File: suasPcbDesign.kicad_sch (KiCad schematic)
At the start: 10 parts, among them U1 LMR51625DDC

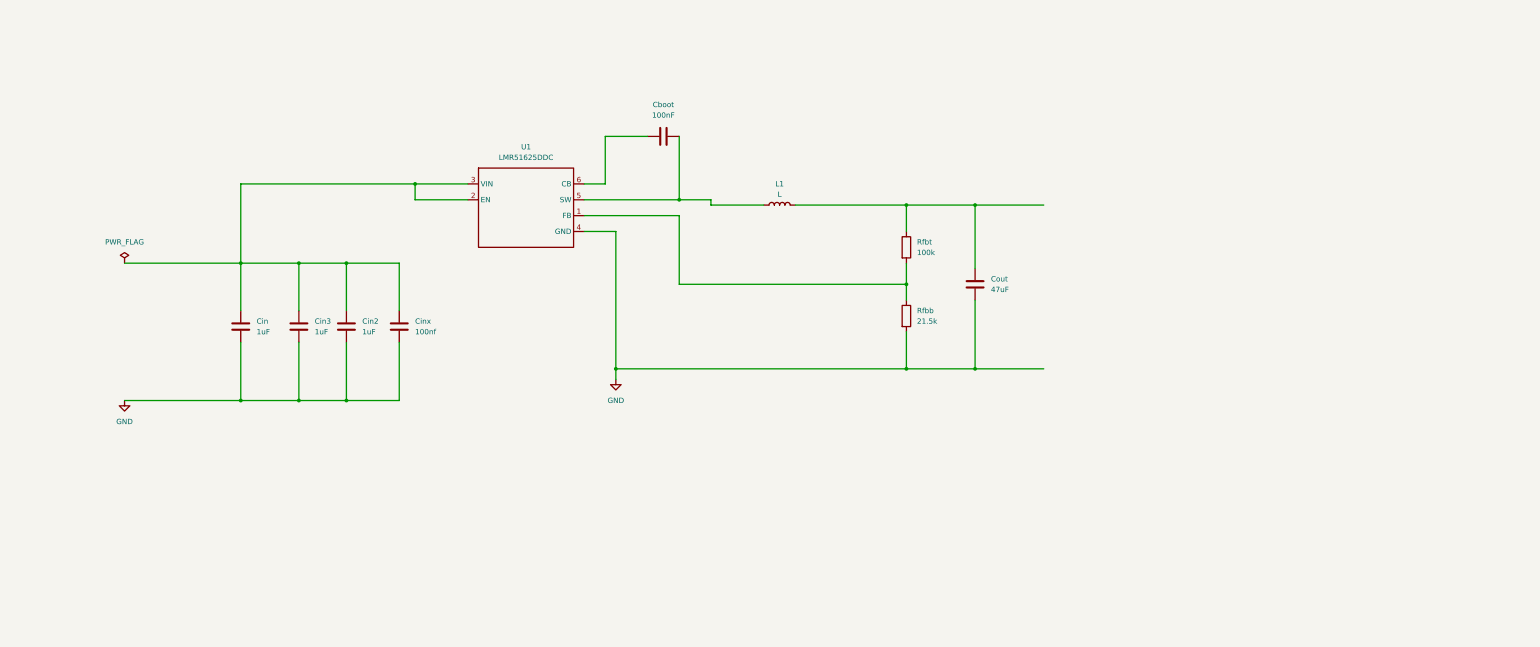
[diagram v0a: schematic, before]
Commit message: added LDO and microcontroller
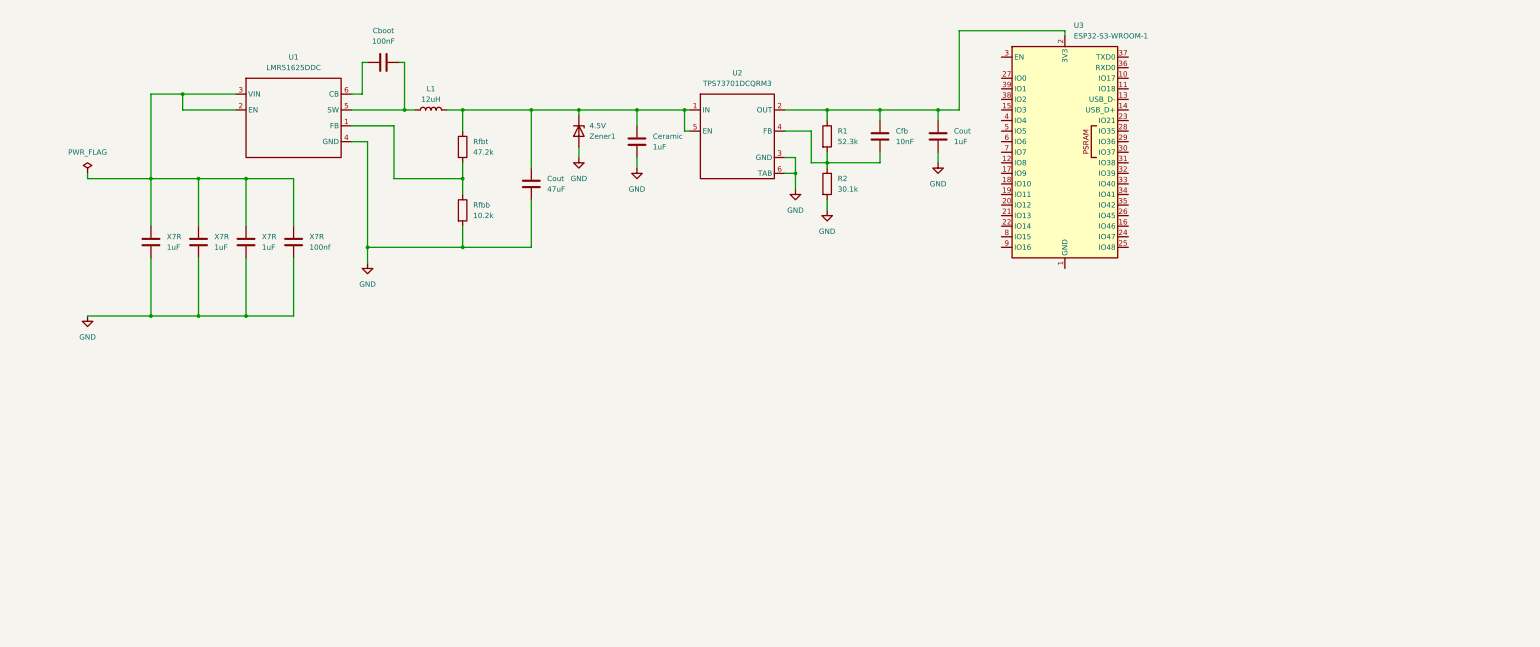
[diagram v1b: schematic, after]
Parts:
- added 4.5V: Zener1, symbol Device:D_Zener
- added Ceramic, Cout: 1uF, symbol Device:C
- added Cfb: 10nF, symbol Device:C
- added R1: 52.3k, symbol Device:R
- added R2: 30.1k, symbol Device:R
- added U2: TPS73701DCQRM3, symbol suasPcbSymbols:TPS73701DCQRM3
- added U3: ESP32-S3-WROOM-1, RF_Module:ESP32-S3-WROOM-1, symbol RF_Module:ESP32-S3-WROOM-1
- L1: value L -> 12uH
- Rfbb: value 21.5k -> 10.2k
- Rfbt: value 100k -> 47.2k
- renumbered Cin2 to X7R, Cin to X7R, Cinx to X7R, Cin3 to X7R
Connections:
- net GND: now also 4.5V.2 (A), Ceramic.2, Cout.2, R2.2, U2.3 (GND), U2.6 (TAB)
- net at Cout.1, L1.2, Rfbt.1: now also 4.5V.1 (K), Ceramic.1, U2.1 (IN), U2.5 (EN)
- new net: Cfb.1, Cout.1, R1.1, U2.2 (OUT), U3.2 (3V3)
- new net: Cfb.2, R1.2, R2.1, U2.4 (FB)
- new net: U3.1 (GND), U3.40 (GND), U3.41 (GND)
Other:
- moved on the sheet: Cboot, Cout, L1, Rfbb, Rfbt, U1, X7R

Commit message: added in zener diode
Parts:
- added Zener2: 3.3V, symbol Device:D_Zener
- Zener1: renamed from 4.5V; value Zener1 -> 4.5V
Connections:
- net GND: now also Zener2.2 (A)
- net at Cfb.1, Cout.1, R1.1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: now also Zener2.1 (K)
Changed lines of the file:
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@@
+	)
+	(junction
+		(at 237.49 29.21)
+		(diameter 0)
+		(color 0 0 0 0)
 	)
 	(junction
@@
 	(wire
 		(pts
+			(xy 237.49 29.21) (xy 237.49 20.32)
+		)
+		(stroke
+			(width 0)
+			(type default)
+		)
+	)
+	(wire
+		(pts
 			(xy 102.87 27.94) (xy 104.14 27.94)
 		)
@@
 	(wire
 		(pts
+			(xy 223.52 29.21) (xy 226.06 29.21)
+		)
+		(stroke
+			(width 0)
+			(type default)
+		)
+	)
+	(wire
+		(pts
 			(xy 171.45 39.37) (xy 171.45 44.45)
 		)
@@
 	(wire
 		(pts
+			(xy 233.68 29.21) (xy 237.49 29.21)
+		)
+		(stroke
+			(width 0)
+			(type default)
+		)
+	)
+	(wire
+		(pts
 			(xy 146.05 48.26) (xy 146.05 50.8)
 		)
@@
 	(wire
 		(pts
-			(xy 237.49 39.37) (xy 237.49 20.32)
+			(xy 237.49 39.37) (xy 237.49 29.21)
 		)
 		(stroke
@@
 	)
 	(symbol
+		(lib_id "Device:D_Zener")
+		(at 229.87 29.21 180)
+		(unit 1)
+		(body_style 1)
+		(exclude_from_sim no)
+		(in_bom yes)
+		(on_board yes)
+		(in_pos_files yes)
+		(dnp no)
+		(fields_autoplaced yes)
+		(property "Reference" "Zener2"
+			(at 229.87 22.86 0)
+			(show_name no)
+			(do_not_autoplace no)
+			(effects
+				(font
+					(size 1.27 1.27)
+				)
+			)
+		)
+		(property "Value" "3.3V"
+			(at 229.87 25.4 0)
+			(show_name no)
+			(do_not_autoplace no)
+			(effects
+				(font
+					(size 1.27 1.27)
+				)
+			)
+		)
+		(property "Footprint" ""
+			(at 229.87 29.21 0)
+			(hide yes)
+			(show_name no)
+			(do_not_autoplace no)
+			(effects
+				(font
+					(size 1.27 1.27)
+				)
+			)
+		)
+		(property "Datasheet" ""
+			(at 229.87 29.21 0)
+			(hide yes)
+			(show_name no)
+			(do_not_autoplace no)
+			(effects
+				(font
+					(size 1.27 1.27)
+				)
+			)
+		)
+		(property "Description" "Zener diode"
+			(at 229.87 29.21 0)
+			(hide yes)
+			(show_name no)
+			(do_not_autoplace no)
+			(effects
+				(font
+					(size 1.27 1.27)
+				)
+			)
+		)
+		(pin "1"
+		)
+		(pin "2"
+		)
+		(instances
+			(project "suasPcbDesign"
+				(path "/3f4829a2-0fac-45c0-b8b3-bdb72c54e399"
+					(reference "Zener2")
+					(unit 1)
+				)
+			)
+		)
+	)
+	(symbol
 		(lib_id "power:GND")
 		(at 160.02 53.34 0)
@@
 		(dnp no)
 		(fields_autoplaced yes)
-		(property "Reference" "4.5V"
+		(property "Reference" "Zener1"
 			(at 148.59 43.1799 90)
 			(show_name no)
@@
 			)
 		)
-		(property "Value" "Zener1"
+		(property "Value" "4.5V"
 			(at 148.59 45.7199 90)
 			(show_name no)
@@
 			(project "suasPcbDesign"
 				(path "/3f4829a2-0fac-45c0-b8b3-bdb72c54e399"
-					(reference "4.5V")
+					(reference "Zener1")
 					(unit 1)
 				)
@@
 					(unit 1)
 				)
+			)
+		)
+	)
+	(symbol
+		(lib_id "power:GND")
+		(at 223.52 29.21 270)
+		(unit 1)
+		(body_style 1)
+		(exclude_from_sim no)
+		(in_bom yes)
+		(on_board yes)
+		(in_pos_files yes)
+		(dnp no)
+		(fields_autoplaced yes)
+		(property "Reference" "#PWR08"
+			(at 217.17 29.21 0)
+			(hide yes)
+			(show_name no)
+			(do_not_autoplace no)
+			(effects
+				(font
+					(size 1.27 1.27)
+				)
+			)
+		)
+		(property "Value" "GND"
+			(at 219.71 29.2099 90)
+			(show_name no)
+			(do_not_autoplace no)
+			(effects
+				(font
+					(size 1.27 1.27)
+				)
+				(justify right)
+			)
+		)
+		(property "Footprint" ""
+			(at 223.52 29.21 0)
+			(hide yes)
+			(show_name no)
+			(do_not_autoplace no)
+			(effects
+				(font
+					(size 1.27 1.27)
+				)
+			)
+		)
+		(property "Datasheet" ""
+			(at 223.52 29.21 0)
+			(hide yes)
+			(show_name no)
+			(do_not_autoplace no)
+			(effects
+				(font
+					(size 1.27 1.27)
+				)
+			)
+		)
+		(property "Description" "Power symbol creates a global label with name \"GND\" , ground"
+			(at 223.52 29.21 0)
+			(hide yes)
+			(show_name no)
+			(do_not_autoplace no)
+			(effects
+				(font
+					(size 1.27 1.27)
+				)
+			)
+		)
+		(pin "1"
+		)
+		(instances
+			(project "suasPcbDesign"
+				(path "/3f4829a2-0fac-45c0-b8b3-bdb72c54e399"
+					(reference "#PWR08")
+					(unit 1)
+				)

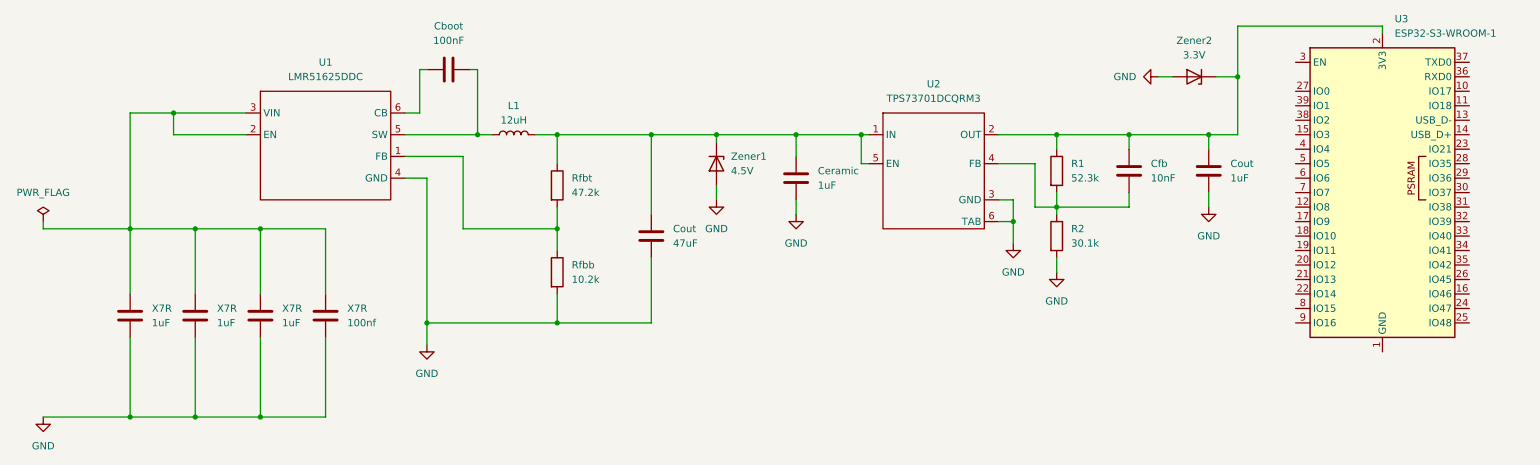
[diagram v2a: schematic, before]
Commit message: Added voltage divider
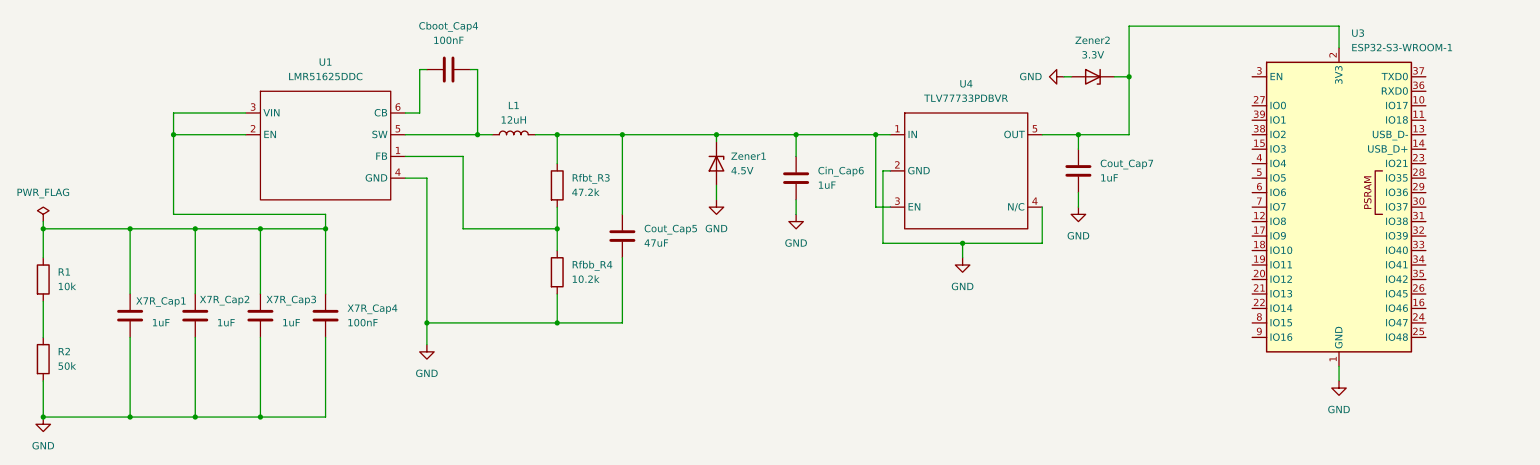
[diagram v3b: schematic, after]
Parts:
- removed Cfb: 10nF, symbol Device:C
- removed U2: TPS73701DCQRM3, symbol suasPcbSymbols:TPS73701DCQRM3
- added U4: TLV77733PDBVR, symbol suasPcbSymbols:TLV77733PDBVR
- R1: value 52.3k -> 10k
- R2: value 30.1k -> 50k
- X7R_Cap4: renamed from X7R; value 100nf -> 100nF
- renumbered Cboot to Cboot_Cap4, Ceramic to Cin_Cap6, Cout to Cout_Cap5, Cout to Cout_Cap7, Rfbb to Rfbb_R4, Rfbt to Rfbt_R3, X7R to X7R_Cap1, X7R to X7R_Cap2, X7R to X7R_Cap3
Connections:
- net GND: now also U3.1 (GND), U3.40 (GND), U3.41 (GND), U4.2 (GND), U4.4 (N/C)
- net at Cin_Cap6.1, Cout_Cap5.1, L1.2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: now also U4.1 (IN), U4.3 (EN)
- net at U1.2 (EN), U1.3 (VIN), X7R_Cap1.1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: now also R1.1
- net at Cout_Cap7.1, U3.2 (3V3), Zener2.1 (K): now also U4.5 (OUT); no longer R1.1
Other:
- moved on the sheet: Cout_Cap5, Cout_Cap7, U3, Zener2

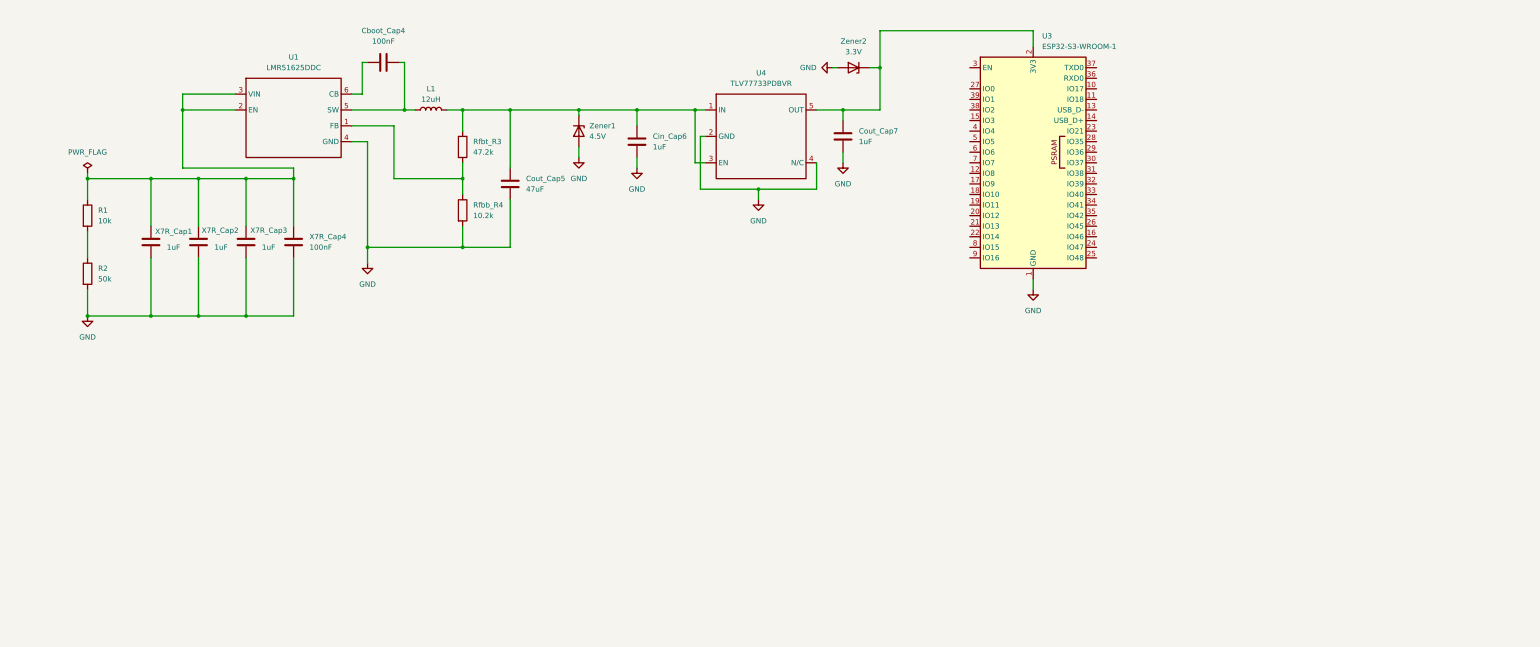
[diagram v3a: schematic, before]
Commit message: Fixed voltage divider and added power to ADC
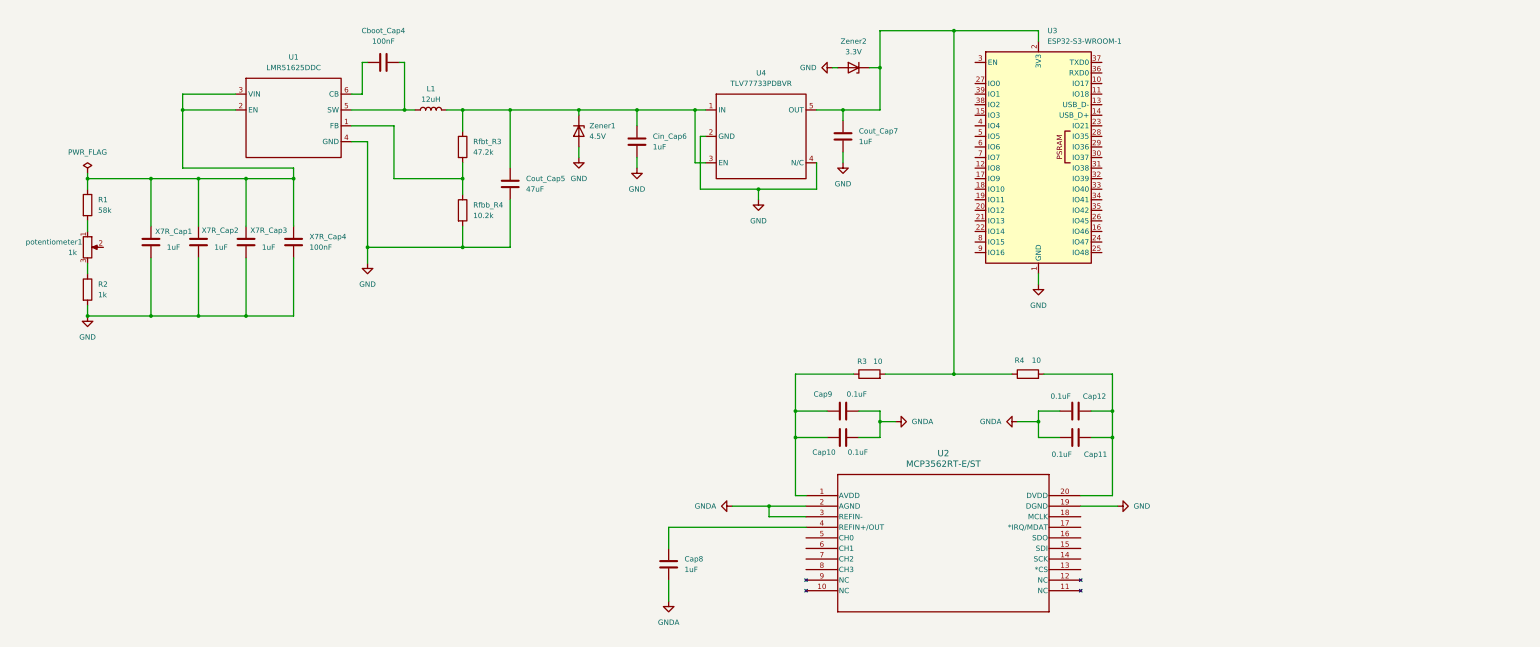
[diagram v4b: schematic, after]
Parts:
- added Cap10, Cap11, Cap12, Cap9: 0.1uF, symbol Device:C
- added Cap8: 1uF, symbol Device:C
- added R3, R4: 10, symbol Device:R
- added U2: MCP3562RT-E/ST, TSSOP20_ST_MCH, symbol suasPcbSymbols:MCP3562RT-E_ST
- added potentiometer1: 1k, symbol Device:R_Potentiometer
- R1: value 10k -> 58k
- R2: value 50k -> 1k
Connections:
- net GND: now also U2.19 (DGND)
- net at R1.2: now also potentiometer1.1; no longer R2.1
- net at Cout_Cap7.1, U3.2 (3V3), U4.5 (OUT)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: now also R3.2, R4.1
- new net: Cap10.1, Cap9.1, R3.1, U2.1 (AVDD)
- new net: Cap11.1, Cap12.1, R4.2, U2.20 (DVDD)
- new net: Cap8.1, U2.4 (REFIN+/OUT)
- new net: R2.1, potentiometer1.3
- new net GNDA: Cap10.2, Cap11.2, Cap12.2, Cap8.2, Cap9.2, U2.2 (AGND), U2.3 (REFIN-)
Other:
- moved on the sheet: R1, R2, U3

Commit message: added current sensor, finished ADC implementation, and added a battery symbol
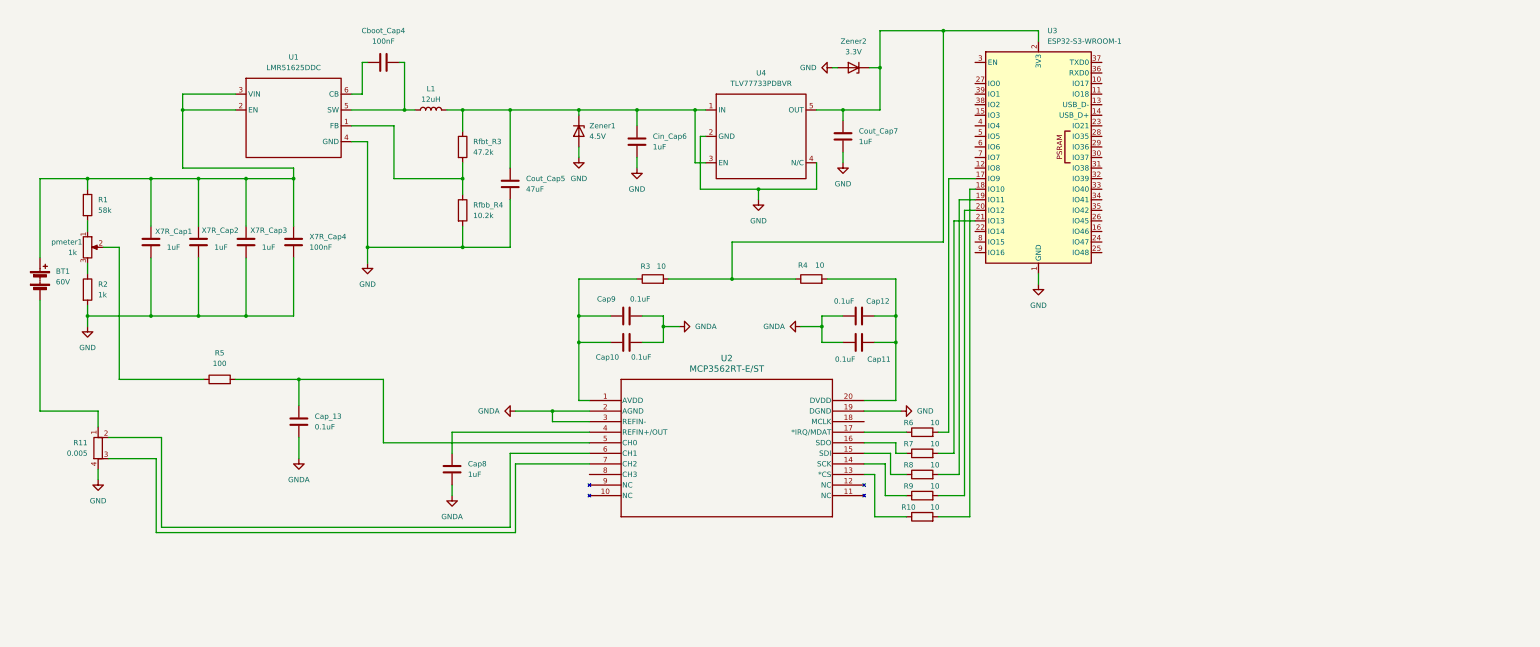
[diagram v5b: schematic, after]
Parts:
- added BT1: 60V, symbol Device:Battery
- added Cap_13: 0.1uF, symbol Device:C
- added R10, R6, R7, R8, R9: 10, symbol Device:R
- added R11: 0.005, symbol Device:R_Shunt
- added R5: 100, symbol Device:R
- renumbered potentiometer1 to pmeter1
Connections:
- net GND: now also R11.4
- net GNDA: now also Cap_13.2
- net at R1.1, U1.2 (EN), U1.3 (VIN)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: now also BT1.1 (+)
- net at U2.13 (*CS): now also R10.1
- net at U2.14 (SCK): now also R9.1
- net at U2.15 (SDI): now also R8.1
- net at U2.16 (SDO): now also R7.1
- net at U2.17 (*IRQ/MDAT): now also R6.1
- net at U2.5 (CH0): now also Cap_13.1, R5.2
- net at U2.6 (CH1): now also R11.2
- net at U2.7 (CH2): now also R11.3
- net at U3.17 (IO9): now also R6.2
- net at U3.18 (IO10): now also R10.2
- net at U3.19 (IO11): now also R8.2
- net at U3.20 (IO12): now also R9.2
- net at U3.21 (IO13): now also R7.2
- net at pmeter1.2: now also R5.1
- new net: BT1.2 (-), R11.1
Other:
- moved on the sheet: Cap10, Cap11, Cap12, Cap8, Cap9, R3, R4, U2
